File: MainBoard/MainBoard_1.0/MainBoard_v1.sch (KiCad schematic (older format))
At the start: 165 parts, among them J1 ILG, J10 SH, J11 SH, J12 SH, J13 FFC, J14 SH, J2 SH, J3 STDC14, J4 PA, J5 Micro_SD_Card_Det_Hirose_DM3AT, J6 SH, J7 ENC, J8 ENC, J9 PA, Q1 AON7400B, Q10 IRLML6344, Q2 AON7400B, Q3 AON7400B, Q4 AON7400B, Q5 AON7400B, Q6 AON7400B, Q7 2N7002K, Q8 AON7400B, Q9 AON7400B, SW1 SKRPACE010, SW2 SSSS213202, SW3 FR01SC16P-S, SW4 SKRHAAE010, U1 SI7469DP-T1-GE3, U10 DRV8701E, U11 MMC5983MA, U2 LT1963A-TSSOP, U3 TPS62143, U4 ECS-2520S33, U5 INA260, U6 DRV8701E, U7 ICM20648, U8 STM32F469VG, U9 INA260

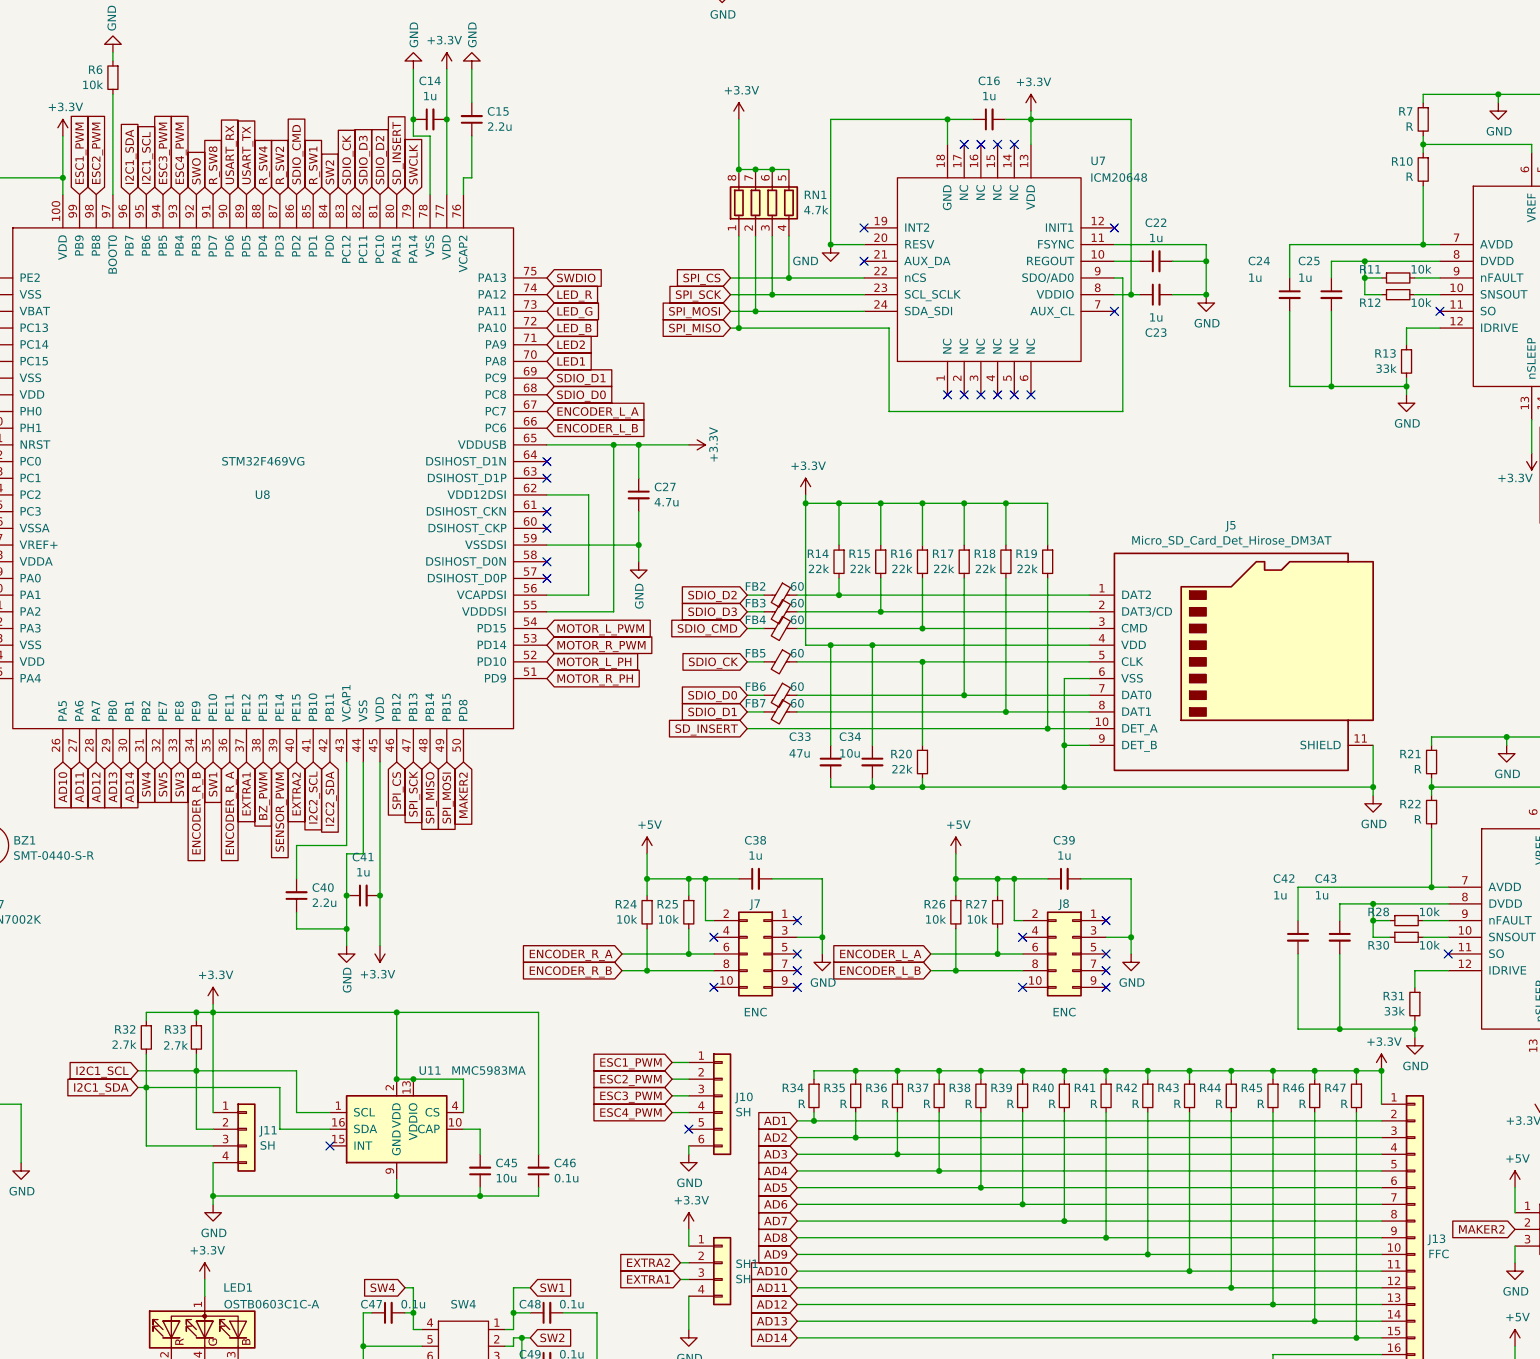
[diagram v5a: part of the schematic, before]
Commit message: センサの抵抗値などを変更
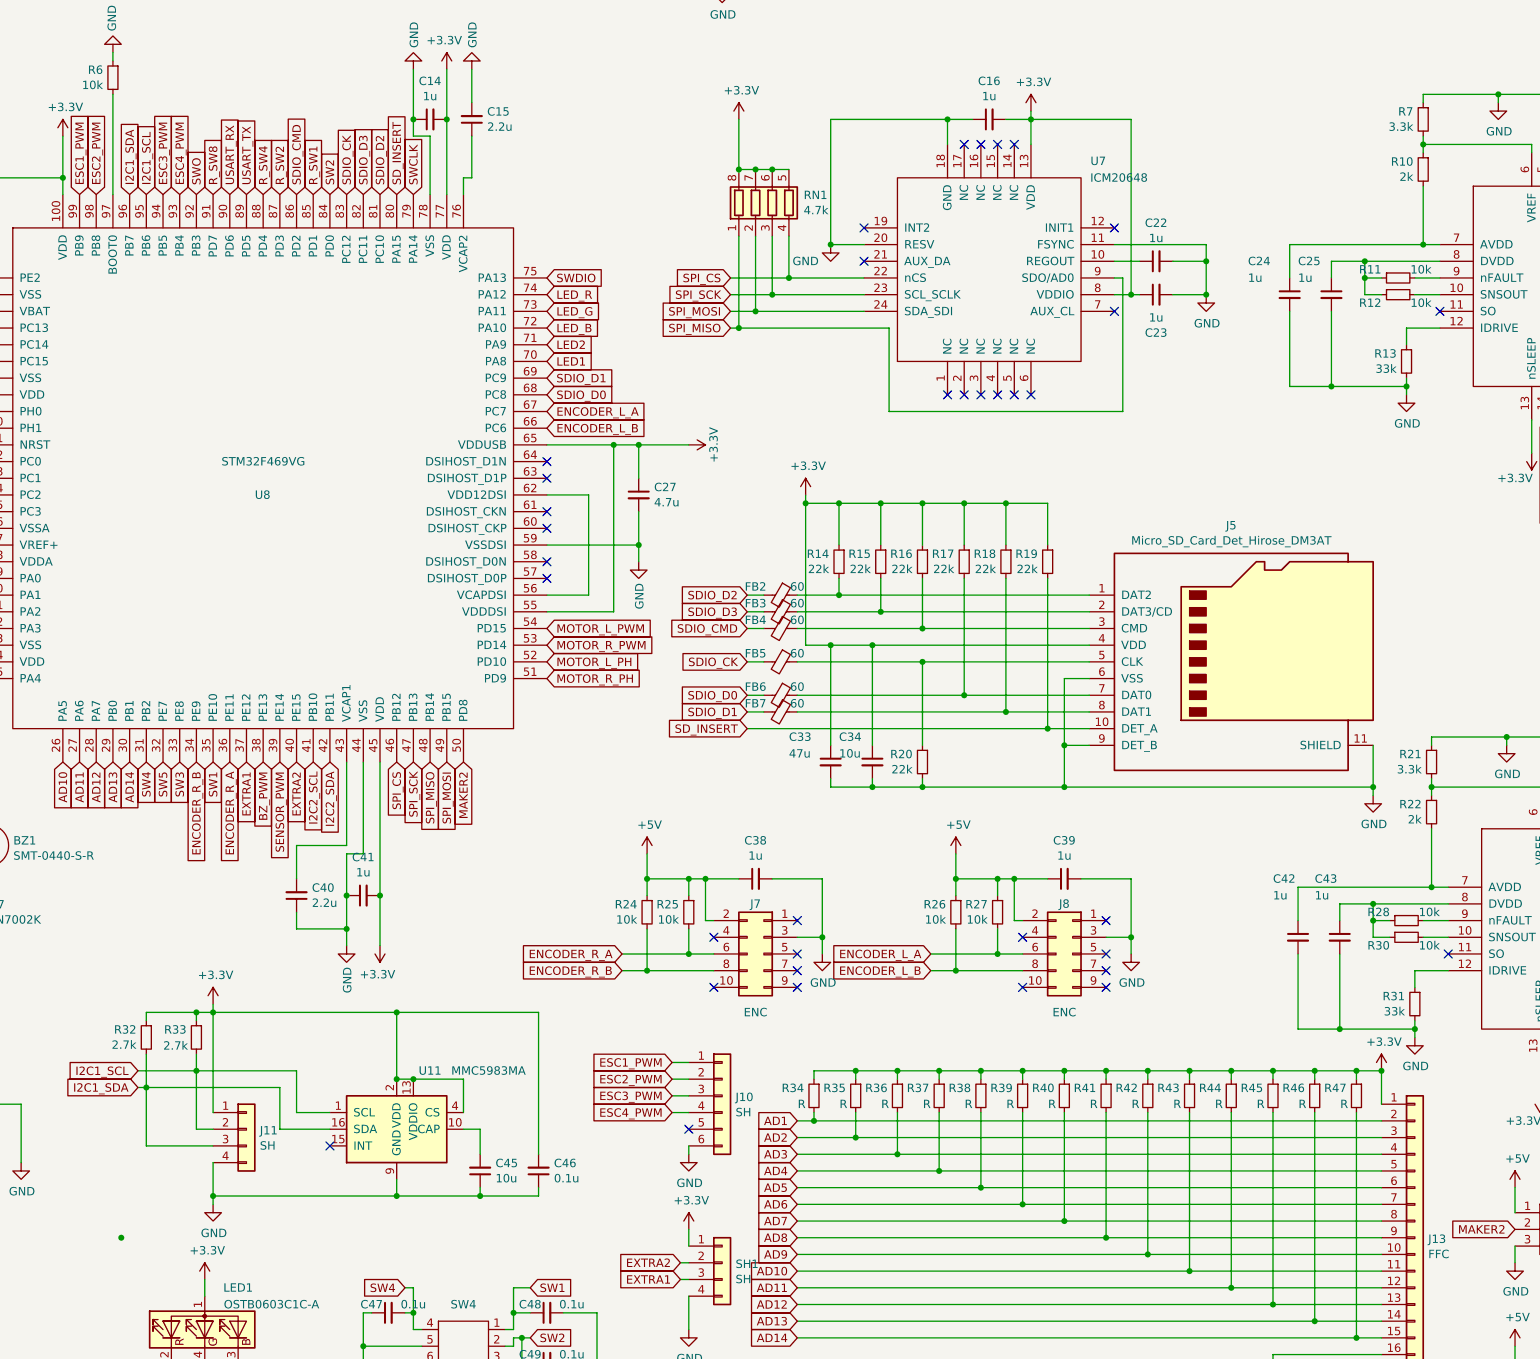
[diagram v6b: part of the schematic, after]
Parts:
- Q1, Q2, Q3, Q4, Q5, Q6, Q8, Q9: footprint Housings_DFN_QFN:DFN-8-1EP_3x3mm_Pitch0.5mm -> Package_DFN_QFN:DFN-8-1EP_3x3mm_P0.65mm_EP1.55x2.4mm
- R10, R22: value R -> 2k
- R21, R7: value R -> 3.3k
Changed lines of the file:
@@
 F 0 "Q1" H 13125 2785 50  0000 C CNN
 F 1 "AON7400B" H 13125 2876 50  0000 C CNN
-F 2 "Housings_DFN_QFN:DFN-8-1EP_3x3mm_Pitch0.5mm" V 13050 3200 50  0001 C CNN
+F 2 "Package_DFN_QFN:DFN-8-1EP_3x3mm_P0.65mm_EP1.55x2.4mm" V 13050 3200 50  0001 C CNN
 F 3 "" V 13050 3200 50  0001 C CNN
 	1    13150 3150
@@
 P 10700 3050
 F 0 "R7" H 10759 3096 50  0000 L CNN
-F 1 "R" H 10759 3005 50  0000 L CNN
+F 1 "3.3k" H 10759 3005 50  0000 L CNN
 F 2 "Resistors_SMD:R_0603" H 10700 3050 50  0001 C CNN
 F 3 "~" H 10700 3050 50  0001 C CNN
@@
 P 10700 3350
 F 0 "R10" H 10759 3396 50  0000 L CNN
-F 1 "R" H 10759 3305 50  0000 L CNN
+F 1 "2k" H 10759 3305 50  0000 L CNN
 F 2 "Resistors_SMD:R_0603" H 10700 3350 50  0001 C CNN
 F 3 "~" H 10700 3350 50  0001 C CNN
@@
 F 0 "Q2" H 13175 3285 50  0000 C CNN
 F 1 "AON7400B" H 13175 3376 50  0000 C CNN
-F 2 "Housings_DFN_QFN:DFN-8-1EP_3x3mm_Pitch0.5mm" V 13100 3700 50  0001 C CNN
+F 2 "Package_DFN_QFN:DFN-8-1EP_3x3mm_P0.65mm_EP1.55x2.4mm" V 13100 3700 50  0001 C CNN
 F 3 "" V 13100 3700 50  0001 C CNN
 	1    13200 3650
@@
 F 0 "Q3" H 13175 4085 50  0000 C CNN
 F 1 "AON7400B" H 13175 4176 50  0000 C CNN
-F 2 "Housings_DFN_QFN:DFN-8-1EP_3x3mm_Pitch0.5mm" V 13100 4500 50  0001 C CNN
+F 2 "Package_DFN_QFN:DFN-8-1EP_3x3mm_P0.65mm_EP1.55x2.4mm" V 13100 4500 50  0001 C CNN
 F 3 "" V 13100 4500 50  0001 C CNN
 	1    13200 4450
@@
 F 0 "Q4" H 13150 4700 50  0000 C CNN
 F 1 "AON7400B" H 13150 4600 50  0000 C CNN
-F 2 "Housings_DFN_QFN:DFN-8-1EP_3x3mm_Pitch0.5mm" V 13050 5000 50  0001 C CNN
+F 2 "Package_DFN_QFN:DFN-8-1EP_3x3mm_P0.65mm_EP1.55x2.4mm" V 13050 5000 50  0001 C CNN
 F 3 "" V 13050 5000 50  0001 C CNN
 	1    13150 4950
@@
 F 0 "Q5" H 13175 6635 50  0000 C CNN
 F 1 "AON7400B" H 13175 6726 50  0000 C CNN
-F 2 "Housings_DFN_QFN:DFN-8-1EP_3x3mm_Pitch0.5mm" V 13100 7050 50  0001 C CNN
+F 2 "Package_DFN_QFN:DFN-8-1EP_3x3mm_P0.65mm_EP1.55x2.4mm" V 13100 7050 50  0001 C CNN
 F 3 "" V 13100 7050 50  0001 C CNN
 	1    13200 7000
@@
 P 10750 6900
 F 0 "R21" H 10809 6946 50  0000 L CNN
-F 1 "R" H 10809 6855 50  0000 L CNN
+F 1 "3.3k" H 10809 6855 50  0000 L CNN
 F 2 "Resistors_SMD:R_0603" H 10750 6900 50  0001 C CNN
 F 3 "~" H 10750 6900 50  0001 C CNN
@@
 P 10750 7200
 F 0 "R22" H 10809 7246 50  0000 L CNN
-F 1 "R" H 10809 7155 50  0000 L CNN
+F 1 "2k" H 10809 7155 50  0000 L CNN
 F 2 "Resistors_SMD:R_0603" H 10750 7200 50  0001 C CNN
 F 3 "~" H 10750 7200 50  0001 C CNN
@@
 F 0 "Q6" H 13225 7135 50  0000 C CNN
 F 1 "AON7400B" H 13225 7226 50  0000 C CNN
-F 2 "Housings_DFN_QFN:DFN-8-1EP_3x3mm_Pitch0.5mm" V 13150 7550 50  0001 C CNN
+F 2 "Package_DFN_QFN:DFN-8-1EP_3x3mm_P0.65mm_EP1.55x2.4mm" V 13150 7550 50  0001 C CNN
 F 3 "" V 13150 7550 50  0001 C CNN
 	1    13250 7500
@@
 F 0 "Q8" H 13225 7935 50  0000 C CNN
 F 1 "AON7400B" H 13225 8026 50  0000 C CNN
-F 2 "Housings_DFN_QFN:DFN-8-1EP_3x3mm_Pitch0.5mm" V 13150 8350 50  0001 C CNN
+F 2 "Package_DFN_QFN:DFN-8-1EP_3x3mm_P0.65mm_EP1.55x2.4mm" V 13150 8350 50  0001 C CNN
 F 3 "" V 13150 8350 50  0001 C CNN
 	1    13250 8300
@@
 F 0 "Q9" H 13200 8550 50  0000 C CNN
 F 1 "AON7400B" H 13200 8450 50  0000 C CNN
-F 2 "Housings_DFN_QFN:DFN-8-1EP_3x3mm_Pitch0.5mm" V 13100 8850 50  0001 C CNN
+F 2 "Package_DFN_QFN:DFN-8-1EP_3x3mm_P0.65mm_EP1.55x2.4mm" V 13100 8850 50  0001 C CNN
 F 3 "" V 13100 8850 50  0001 C CNN
 	1    13200 8800
@@
 NoConn ~ 4450 1750
 NoConn ~ 4950 1750
+Connection ~ 2900 9750
 $EndSCHEMATC
